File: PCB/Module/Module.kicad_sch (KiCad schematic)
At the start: 22 parts, among them J1 SWD_Programmer, U1 PY32F002BF15P6TU, U2 PinHeaderTop, U3 PinHeaderRight, U4 PinHeaderBottom, U5 PinHeaderLeft, U6 Button

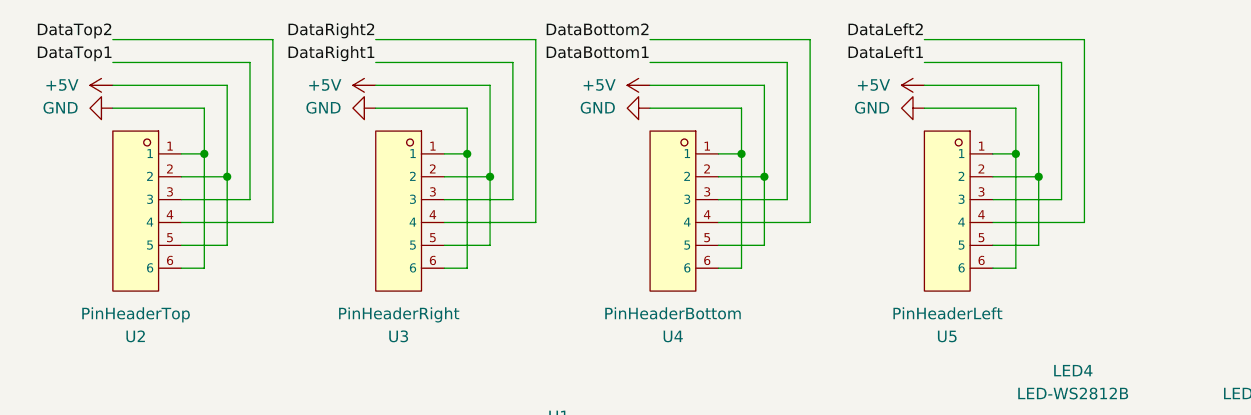
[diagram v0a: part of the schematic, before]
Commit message: Prevent accidental short circuit and add basic box 3d model freecad
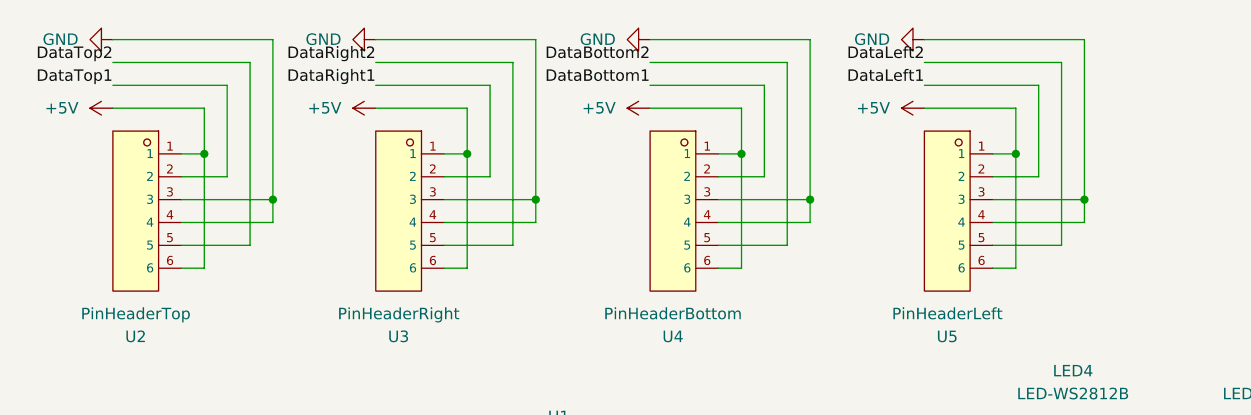
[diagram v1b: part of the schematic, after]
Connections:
- net +5V: now also U2.1, U2.6, U3.1, U3.6, U4.1, U4.6, U5.1, U5.6; no longer U2.2, U2.5, U3.2, U3.5, U4.2, U4.5, U5.2, U5.5
- net DataBottom1: now also U4.2; no longer U4.3
- net DataBottom2: now also U4.5; no longer U4.4
- net DataLeft1: now also U5.2; no longer U5.3
- net DataLeft2: now also U5.5; no longer U5.4
- net DataRight1: now also U3.2; no longer U3.3
- net DataRight2: now also U3.5; no longer U3.4
- net DataTop1: now also U2.2; no longer U2.3
- net DataTop2: now also U2.5; no longer U2.4
- net GND: now also U2.3, U2.4, U3.3, U3.4, U4.3, U4.4, U5.3, U5.4; no longer U2.1, U2.6, U3.1, U3.6, U4.1, U4.6, U5.1, U5.6

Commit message: Update PCB
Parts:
- removed LED1, LED2, LED3, LED4: LED-WS2812B, CustomFootprints:LED-WS2812B, symbol Custom_Parts:LED-WS2812B
- removed R9: 10k, Resistor_SMD:R_0402_1005Metric, symbol Device:R
- removed U6: Button, CustomFootprints:Button, symbol Custom_Parts:Button
- added J2: Shield_Connector_Top_Right, Connector_PinSocket_2.54mm:PinSocket_1x01_P2.54mm_Vertical, symbol Connector_Generic:Conn_01x01
- added J3: Shield_Connector_Bottom_Right, Connector_PinSocket_2.54mm:PinSocket_1x01_P2.54mm_Vertical, symbol Connector_Generic:Conn_01x01
- added J4: Shield_Connector_Top_Left, Connector_PinSocket_2.54mm:PinSocket_1x01_P2.54mm_Vertical, symbol Connector_Generic:Conn_01x01
- added J5: Shield_Connector_Bottom_Left, Connector_PinSocket_2.54mm:PinSocket_1x01_P2.54mm_Vertical, symbol Connector_Generic:Conn_01x01
- added LED1, LED2, LED3, LED4: SK6812MINI-HS, CustomFootprints:LED-SK6812MINI-HS, symbol Custom_Parts:SK6812MINI-HS
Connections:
- net +5V: now also LED1.3 (VDD), LED2.3 (VDD), LED3.3 (VDD), LED4.3 (VDD)
- net DataRight1: now also U1.12 (PB3); no longer U1.10 (PB5)
- net GND: now also LED1.1 (GND), LED2.1 (GND), LED3.1 (GND), LED4.1 (GND)
- net LedIn: now also LED1.2 (DIN)
- net ShieldTopRight: now reaches U1.13 (PB2)
- net ShieldTopRight: now also J2.1 (Pin_1)
- net ShieldBottomLeft: now reaches U1.2 (PA6)
- net ShieldBottomLeft: now also J5.1 (Pin_1)
- net ButtonRead renamed ShieldTopLeft
- net ShieldTopLeft: now also J4.1 (Pin_1)
- new net: LED3.4 (DOUT), LED4.2 (DIN)
- new net: LED1.4 (DOUT), LED2.2 (DIN)
- new net: LED2.4 (DOUT), LED3.2 (DIN)
- new net ShieldBottomRight: J3.1 (Pin_1), U1.10 (PB5)
- no-connect marks 6 -> 3
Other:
- moved on the sheet: C1, C2

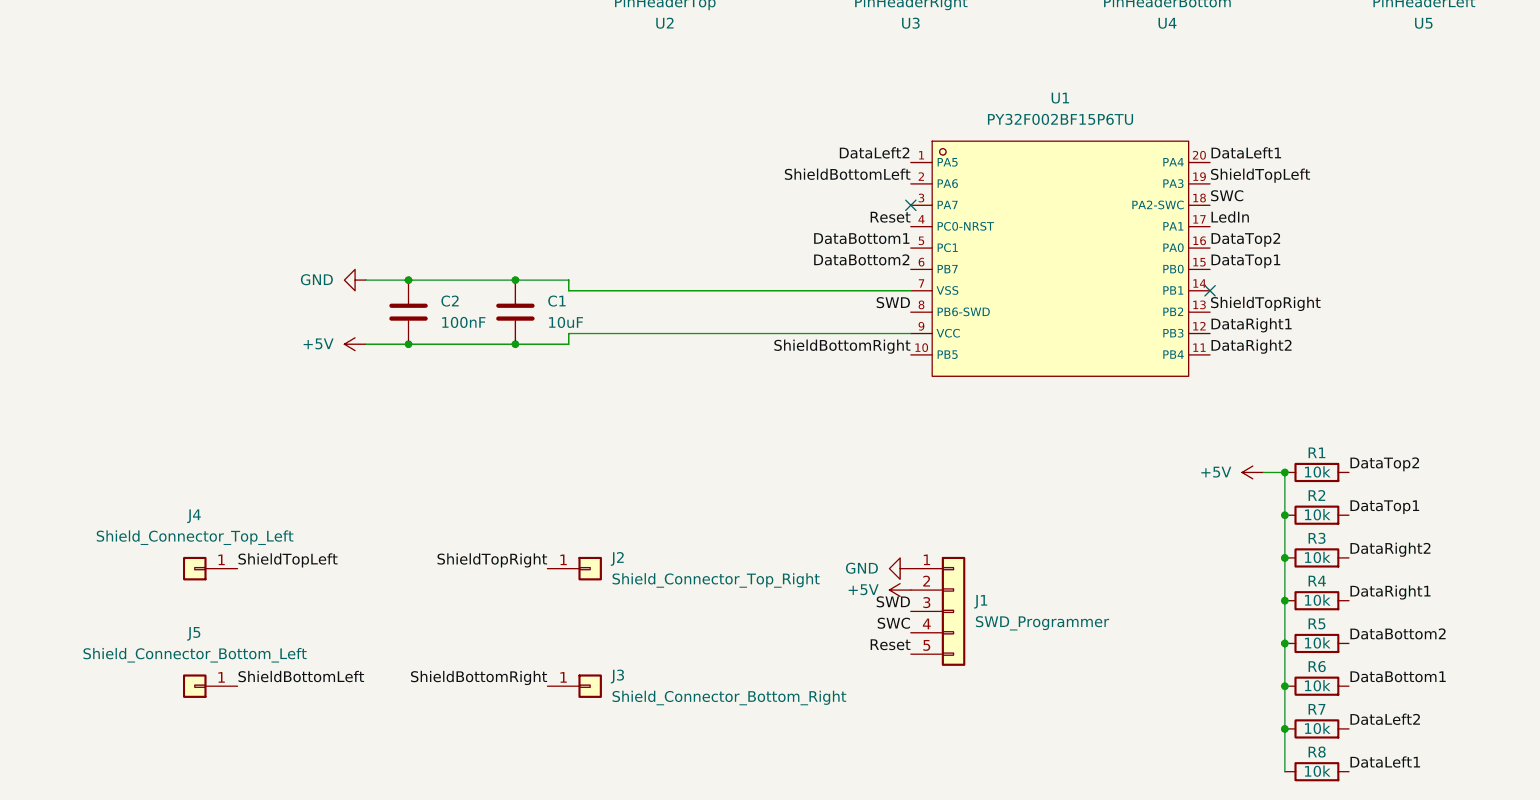
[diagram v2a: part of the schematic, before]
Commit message: Add hall sensor shield
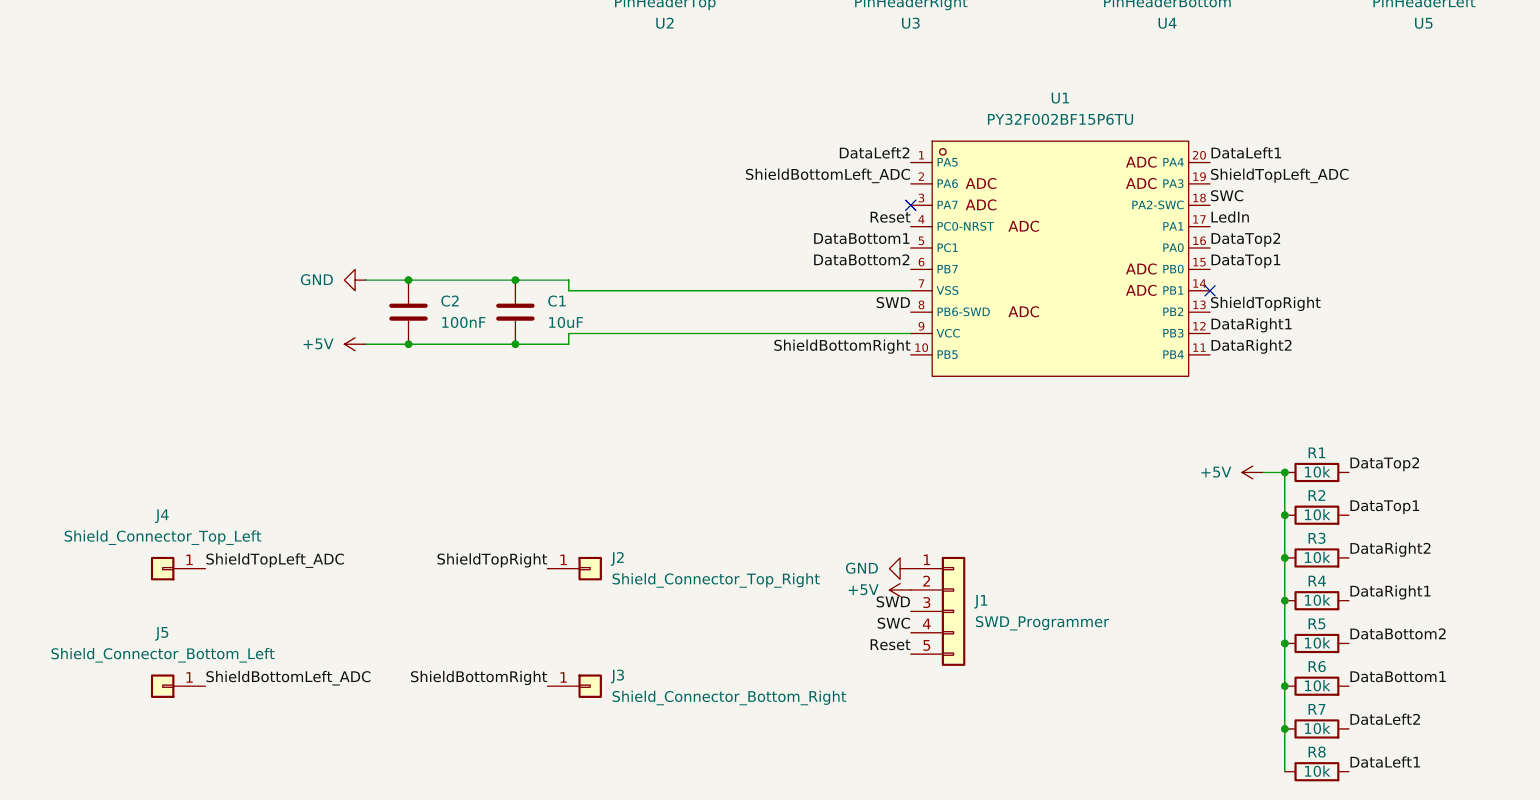
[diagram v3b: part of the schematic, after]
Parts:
- J2, J3, J4, J5: footprint Connector_PinSocket_2.54mm:PinSocket_1x01_P2.54mm_Vertical -> CustomFootprints:HDR-TH_1P-V-F-1
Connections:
- net ShieldBottomLeft renamed ShieldBottomLeft_ADC
- net ShieldTopLeft renamed ShieldTopLeft_ADC
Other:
- moved on the sheet: J4, J5
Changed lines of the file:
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@@
 		)
 	)
-	(label "ShieldTopLeft"
-		(at 46.99 120.65 0)
+	(label "ShieldTopLeft_ADC"
+		(at 43.18 120.65 0)
 		(effects
 			(font
@@
 		)
 	)
-	(label "ShieldBottomLeft"
+	(label "ShieldBottomLeft_ADC"
 		(at 127 74.93 180)
 		(effects
@@
 		)
 	)
-	(label "ShieldBottomLeft"
-		(at 46.99 134.62 0)
+	(label "ShieldBottomLeft_ADC"
+		(at 43.18 134.62 0)
 		(effects
 			(font
@@
 		)
 	)
-	(label "ShieldTopLeft"
+	(label "ShieldTopLeft_ADC"
 		(at 162.56 74.93 0)
 		(effects
@@
 	(symbol
 		(lib_id "Connector_Generic:Conn_01x01")
-		(at 41.91 120.65 180)
+		(at 38.1 120.65 180)
 		(unit 1)
 		(exclude_from_sim no)
@@
 		(fields_autoplaced yes)
 		(property "Reference" "J4"
-			(at 41.91 114.3 0)
+			(at 38.1 114.3 0)
 			(effects
 				(font
@@
 		)
 		(property "Value" "Shield_Connector_Top_Left"
-			(at 41.91 116.84 0)
-			(effects
-				(font
-					(size 1.27 1.27)
-				)
-			)
-		)
-		(property "Footprint" "Connector_PinSocket_2.54mm:PinSocket_1x01_P2.54mm_Vertical"
-			(at 41.91 120.65 0)
+			(at 38.1 116.84 0)
+			(effects
+				(font
+					(size 1.27 1.27)
+				)
+			)
+		)
+		(property "Footprint" "CustomFootprints:HDR-TH_1P-V-F-1"
+			(at 38.1 120.65 0)
 			(effects
 				(font
@@
 		)
 		(property "Datasheet" "~"
-			(at 41.91 120.65 0)
+			(at 38.1 120.65 0)
 			(effects
 				(font
@@
 		)
 		(property "Description" "Generic connector, single row, 01x01, script generated (kicad-library-utils/schlib/autogen/connector/)"
-			(at 41.91 120.65 0)
+			(at 38.1 120.65 0)
 			(effects
 				(font
@@
 			)
 		)
-		(property "Footprint" "Connector_PinSocket_2.54mm:PinSocket_1x01_P2.54mm_Vertical"
+		(property "Footprint" "CustomFootprints:HDR-TH_1P-V-F-1"
 			(at 88.9 120.65 0)
 			(effects
@@
 			)
 		)
-		(property "Footprint" "Connector_PinSocket_2.54mm:PinSocket_1x01_P2.54mm_Vertical"
+		(property "Footprint" "CustomFootprints:HDR-TH_1P-V-F-1"
 			(at 88.9 134.62 0)
 			(effects
@@
 	(symbol
 		(lib_id "Connector_Generic:Conn_01x01")
-		(at 41.91 134.62 180)
+		(at 38.1 134.62 180)
 		(unit 1)
 		(exclude_from_sim no)
@@
 		(fields_autoplaced yes)
 		(property "Reference" "J5"
-			(at 41.91 128.27 0)
+			(at 38.1 128.27 0)
 			(effects
 				(font
@@
 		)
 		(property "Value" "Shield_Connector_Bottom_Left"
-			(at 41.91 130.81 0)
-			(effects
-				(font
-					(size 1.27 1.27)
-				)
-			)
-		)
-		(property "Footprint" "Connector_PinSocket_2.54mm:PinSocket_1x01_P2.54mm_Vertical"
-			(at 41.91 134.62 0)
+			(at 38.1 130.81 0)
+			(effects
+				(font
+					(size 1.27 1.27)
+				)
+			)
+		)
+		(property "Footprint" "CustomFootprints:HDR-TH_1P-V-F-1"
+			(at 38.1 134.62 0)
 			(effects
 				(font
@@
 		)
 		(property "Datasheet" "~"
-			(at 41.91 134.62 0)
+			(at 38.1 134.62 0)
 			(effects
 				(font
@@
 		)
 		(property "Description" "Generic connector, single row, 01x01, script generated (kicad-library-utils/schlib/autogen/connector/)"
-			(at 41.91 134.62 0)
-			(effects
-				(font
+			(at 38.1 134.62 0)
+			(effects
+				(font

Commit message: Add power supply (wip) and update panel
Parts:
- J2, J3, J4, J5: LCSC (none) -> C2883469
- U2, U3, U4, U5: now in the parts list
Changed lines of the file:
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@@
+			)
+		)
+		(property "LCSC" "C2883469"
+			(at 38.1 120.65 0)
+			(effects
+				(font
+					(size 1.27 1.27)
+				)
+				(hide yes)
 			)
 		)
@@
 		(unit 1)
 		(exclude_from_sim no)
-		(in_bom no)
+		(in_bom yes)
 		(on_board yes)
 		(dnp no)
@@
 			)
 		)
+		(property "LCSC" "C2883469"
+			(at 88.9 120.65 0)
+			(effects
+				(font
+					(size 1.27 1.27)
+				)
+				(hide yes)
+			)
+		)
 		(pin "1"
 		)
@@
 		(unit 1)
 		(exclude_from_sim no)
-		(in_bom no)
+		(in_bom yes)
 		(on_board yes)
 		(dnp no)
@@
 		(unit 1)
 		(exclude_from_sim no)
-		(in_bom no)
+		(in_bom yes)
 		(on_board yes)
 		(dnp no)
@@
 			)
 		)
+		(property "LCSC" "C2883469"
+			(at 88.9 134.62 0)
+			(effects
+				(font
+					(size 1.27 1.27)
+				)
+				(hide yes)
+			)
+		)
 		(pin "1"
 		)
@@
 		(unit 1)
 		(exclude_from_sim no)
-		(in_bom no)
+		(in_bom yes)
 		(on_board yes)
 		(dnp no)
@@
 			(at 38.1 134.62 0)
 			(effects
+				(font
+					(size 1.27 1.27)
+				)
+				(hide yes)
+			)
+		)
+		(property "LCSC" "C2883469"
+			(at 38.1 134.62 0)
+			(effects
